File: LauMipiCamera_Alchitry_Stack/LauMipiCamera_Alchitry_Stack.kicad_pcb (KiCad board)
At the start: 2 copper layers, 55 x 45 mm, 19 parts, among them J1 DF40C-50DP (Site A / +3V3 onl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, J2 DF40C-80DP (Bank A / Site B /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, J3 DF40C-80DP (Bank B / Site C), SW1 SW_DIP_x4

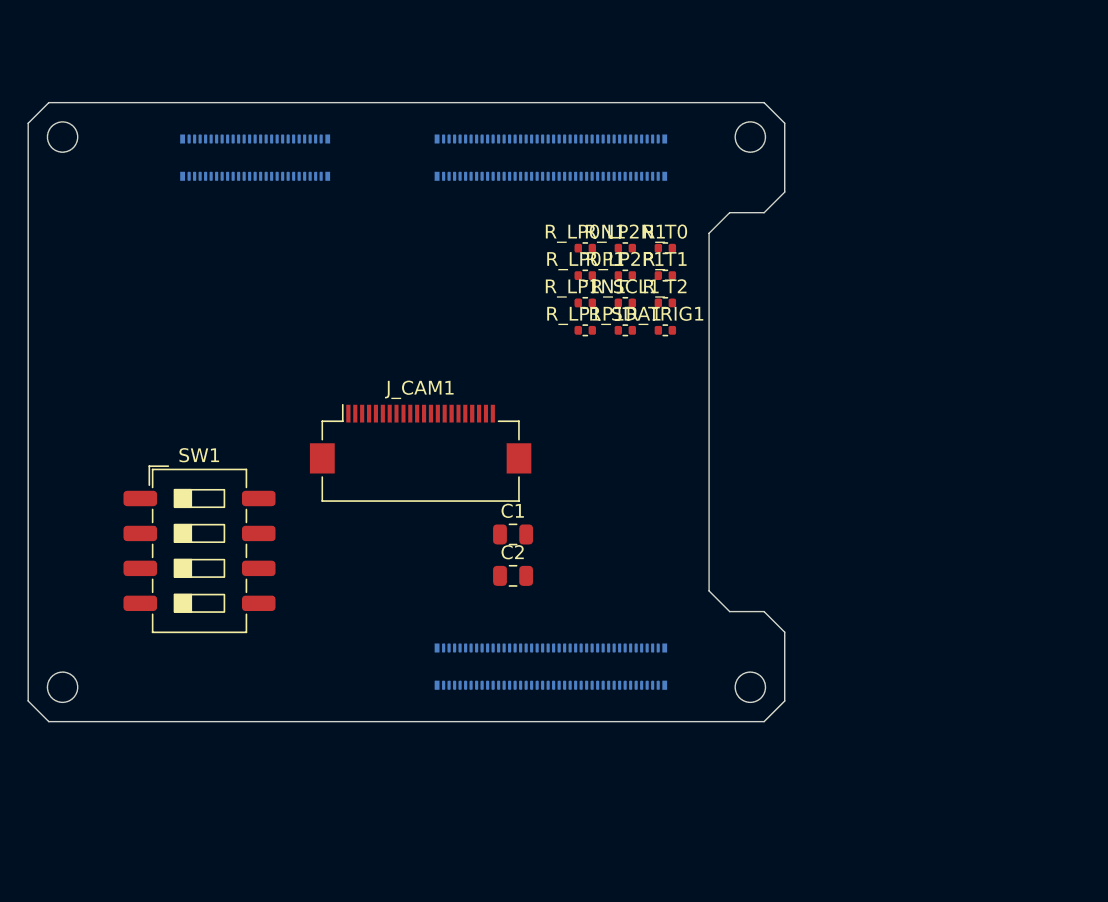
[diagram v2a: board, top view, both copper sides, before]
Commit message: hw(mipi): 4-layer stackup, 100R diff geometry, GND pours
Prerequisite for routing the D-PHY pairs. The board was 2-layer with no stackup
and no ground pour, so the HS pairs had no reference plane and 100 ohm
differential was unachievable (1.6 mm core would need ~1 mm traces, which cannot
escape a 0.4 mm-pitch DF40 fanout).

Stackup (generic 1.6 mm 4-layer, 1.62 mm with masks):
  F.Cu    35 um   signal   <- HS pairs, microstrip
    prepreg 0.0994 mm, er 4.45
  In1.Cu  15.2 um GND      <- reference plane
    core 1.3008 mm, er 4.6
  In2.Cu  15.2 um GND
    prepreg 0.0994 mm, er 4.45
  B.Cu    35 um   signal   <- DF40 plugs J1/J2/J3

100 ohm differential over that prepreg: trace 0.10 mm, gap 0.13 mm. Hammerstad
microstrip + Wadell coupling gives Zdiff = 101.9 ohm bare; solder mask pulls it
down ~2 ohm. Replaces the 0.13/0.13 placeholders in both .kicad_dru and the
MipiHS netclass. MUST still be confirmed against the fab's own stackup.

Added GND pours on all four layers (In1 highest priority -- it is the HS
reference). Zones are defined but not filled; fill in the GUI.

Also re-applied the MipiHS netclass clearance 0.2 -> 0.15 mm. KiCad had reverted
it when the project was saved from the GUI, which would have re-broken DRC
against the DF40's fixed 0.17 mm pad gap.

Documented in .kicad_dru that exactly ONE via per HS net is expected: J_CAM1 is
on F.Cu and J3 on B.Cu, so each pair drops through once near J3, swapping its
reference from In1 to In2 -- needs a GND stitching via beside each transition.

DRC: 0 copper violations, schematic_parity 0. 46 remaining are silkscreen.

Co-Authored-By: Claude Opus 4.8 (1M context) <noreply@anthropic.com>
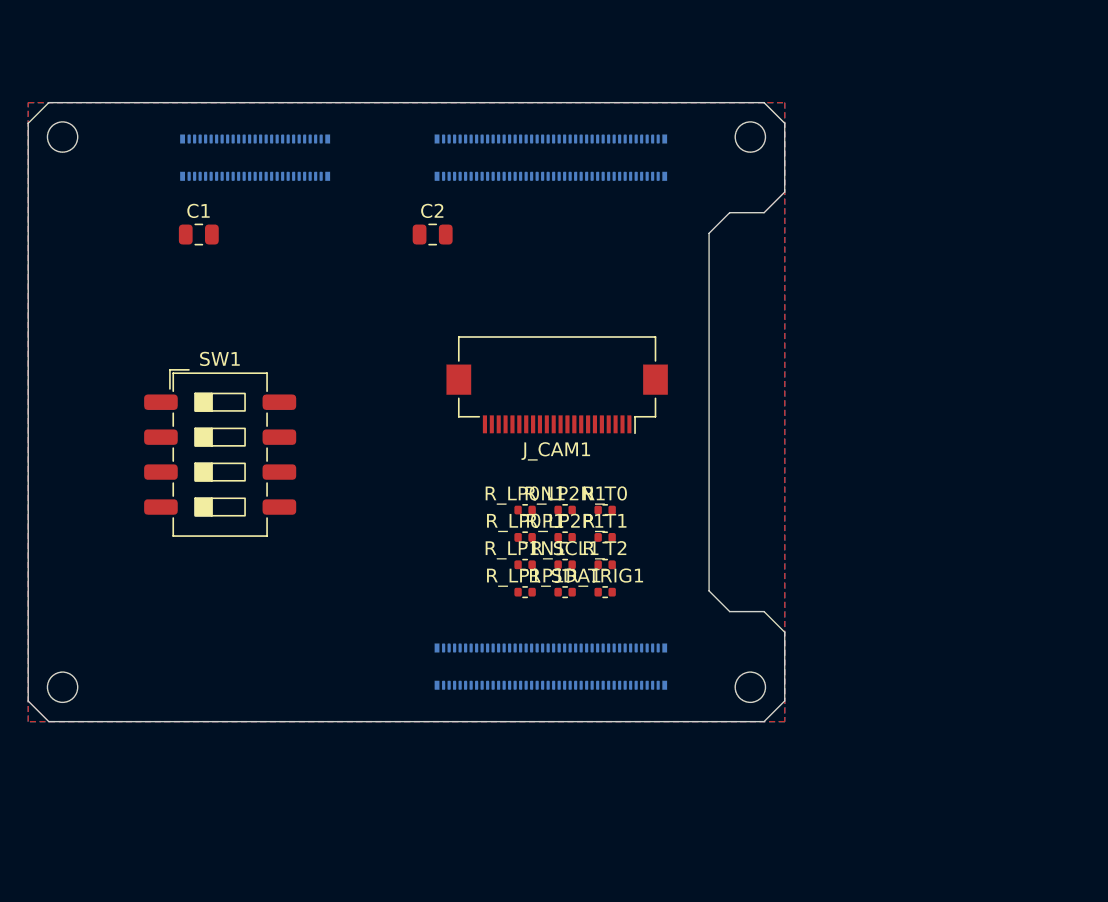
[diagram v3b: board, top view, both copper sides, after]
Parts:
- moved C1 31.6 mm to (131.9, 70.0)
- moved C2 25.5 mm to (148.9, 70.0)
- moved R_LP1N1 19.5 mm to (155.7, 94.0)
- moved R_SCL1 19.5 mm to (158.6, 94.0)
- moved R_T2 19.5 mm to (161.5, 94.0)
- moved R_LP0N1 19.5 mm to (155.7, 90.0)
- moved R_LP0P1 19.5 mm to (155.7, 92.0)
- moved R_LP1P1 19.5 mm to (155.7, 96.0)
- moved R_LP2N1 19.5 mm to (158.6, 90.0)
- moved R_LP2P1 19.5 mm to (158.6, 92.0)
- moved R_SDA1 19.5 mm to (158.6, 96.0)
- moved R_T0 19.5 mm to (161.5, 90.0)
- moved R_T1 19.5 mm to (161.5, 92.0)
- moved R_TRIG1 19.5 mm to (161.5, 96.0)
- moved J_CAM1 10.3 mm to (158.0, 82.0), turned to 180 degrees
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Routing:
- added copper zone on B.Cu, net GND
- added copper zone on F.Cu, net GND
- added copper zone on In1.Cu, net GND
- added copper zone on In2.Cu, net GND
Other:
- copper layers 2 -> 4

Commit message: hw(mipi): rotate J_CAM1 180 deg so the HS pairs stop crossing
All three D-PHY pairs crossed between the camera and J3:

  lane  at J_CAM1            at J3                verdict
  CK    P=159.25 N=159.75    P=158.94 N=158.54    P-left  vs P-right
  D0    P=162.25 N=162.75    P=157.75 N=157.34    P-left  vs P-right
  D1    P=160.75 N=161.25    P=158.94 N=158.54    P-left  vs P-right

Systematic, not a per-lane slip: J_CAM1 was at rot=180 so its pin numbers ran
right-to-left, while J3's run left-to-right. The FPGA side cannot absorb this --
on the DF40 the higher B-number is always the P ball (CK = B47/B45 -> V13/V14,
V13 = P; the spare MRCC pair B41/B39 has the same parity), so P is always to the
right. Swapping P/N in the schematic would land the camera's P on the FPGA's N.

Routing as-placed would need a crossover via on one leg of each pair: three
discontinuities mid-line on a 200 mV 691 Mb/s link, and it breaks the symmetry
that makes the 0.08 mm intra-pair skew constraint free.

Rotating J_CAM1 to rot=0 mirrors its pads about x=158. P now sits right of N on
all three lanes, matching J3, so each pair can be routed symmetric about its own
centreline and intra-pair skew is zero by construction. Cost: ~3.7 mm more run
per lane (camera pads y 83.80 -> 80.10) and the FFC cable exits the other side.

Also cleared the 180 deg self-rotation left on the 24 child pads, which had made
the footprint differ from its library copy (geometrically identical for rect
pads, but it raised lib_footprint_mismatch).

DRC: 0 copper violations, schematic_parity 0, 46 silkscreen.

Co-Authored-By: Claude Opus 4.8 (1M context) <noreply@anthropic.com>
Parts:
- turned J_CAM1 to 0 degrees
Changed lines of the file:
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@@
 	(footprint "Connector_FFC-FPC:Hirose_FH12-22S-0.5SH_1x22-1MP_P0.50mm_Horizontal"
 		(layer "F.Cu")
-		(at 158 81.95 180)
+		(at 158 81.95)
 		(descr "Hirose FH12, FFC/FPC connector, FH12-22S-0.5SH, 22 Pins per row (https://www.hirose.com/product/en/products/FH12/FH12-24S-0.5SH(55)/)")
 		(tags "connector Hirose FH12 horizontal")
@@
 		)
 		(pad "1" smd rect
-			(at -5.25 -1.85 180)
+			(at -5.25 -1.85)
 			(size 0.3 1.3)
 			(layers "F.Cu" "F.Mask" "F.Paste")
@@
 		)
 		(pad "2" smd rect
-			(at -4.75 -1.85 180)
+			(at -4.75 -1.85)
 			(size 0.3 1.3)
 			(layers "F.Cu" "F.Mask" "F.Paste")
@@
 		)
 		(pad "3" smd rect
-			(at -4.25 -1.85 180)
+			(at -4.25 -1.85)
 			(size 0.3 1.3)
 			(layers "F.Cu" "F.Mask" "F.Paste")
@@
 		)
 		(pad "4" smd rect
-			(at -3.75 -1.85 180)
+			(at -3.75 -1.85)
 			(size 0.3 1.3)
 			(layers "F.Cu" "F.Mask" "F.Paste")
@@
 		)
 		(pad "5" smd rect
-			(at -3.25 -1.85 180)
+			(at -3.25 -1.85)
 			(size 0.3 1.3)
 			(layers "F.Cu" "F.Mask" "F.Paste")
@@
 		)
 		(pad "6" smd rect
-			(at -2.75 -1.85 180)
+			(at -2.75 -1.85)
 			(size 0.3 1.3)
 			(layers "F.Cu" "F.Mask" "F.Paste")
@@
 		)
 		(pad "7" smd rect
-			(at -2.25 -1.85 180)
+			(at -2.25 -1.85)
 			(size 0.3 1.3)
 			(layers "F.Cu" "F.Mask" "F.Paste")
@@
 		)
 		(pad "8" smd rect
-			(at -1.75 -1.85 180)
+			(at -1.75 -1.85)
 			(size 0.3 1.3)
 			(layers "F.Cu" "F.Mask" "F.Paste")
@@
 		)
 		(pad "9" smd rect
-			(at -1.25 -1.85 180)
+			(at -1.25 -1.85)
 			(size 0.3 1.3)
 			(layers "F.Cu" "F.Mask" "F.Paste")
@@
 		)
 		(pad "10" smd rect
-			(at -0.75 -1.85 180)
+			(at -0.75 -1.85)
 			(size 0.3 1.3)
 			(layers "F.Cu" "F.Mask" "F.Paste")
@@
 		)
 		(pad "11" smd rect
-			(at -0.25 -1.85 180)
+			(at -0.25 -1.85)
 			(size 0.3 1.3)
 			(layers "F.Cu" "F.Mask" "F.Paste")
@@
 		)
 		(pad "12" smd rect
-			(at 0.25 -1.85 180)
+			(at 0.25 -1.85)
 			(size 0.3 1.3)
 			(layers "F.Cu" "F.Mask" "F.Paste")
@@
 		)
 		(pad "13" smd rect
-			(at 0.75 -1.85 180)
+			(at 0.75 -1.85)
 			(size 0.3 1.3)
 			(layers "F.Cu" "F.Mask" "F.Paste")
@@
 		)
 		(pad "14" smd rect
-			(at 1.25 -1.85 180)
+			(at 1.25 -1.85)
 			(size 0.3 1.3)
 			(layers "F.Cu" "F.Mask" "F.Paste")
@@
 		)
 		(pad "15" smd rect
-			(at 1.75 -1.85 180)
+			(at 1.75 -1.85)
 			(size 0.3 1.3)
 			(layers "F.Cu" "F.Mask" "F.Paste")
@@
 		)
 		(pad "16" smd rect
-			(at 2.25 -1.85 180)
+			(at 2.25 -1.85)
 			(size 0.3 1.3)
 			(layers "F.Cu" "F.Mask" "F.Paste")
@@
 		)
 		(pad "17" smd rect
-			(at 2.75 -1.85 180)
+			(at 2.75 -1.85)
 			(size 0.3 1.3)
 			(layers "F.Cu" "F.Mask" "F.Paste")
@@
 		)
 		(pad "18" smd rect
-			(at 3.25 -1.85 180)
+			(at 3.25 -1.85)
 			(size 0.3 1.3)
 			(layers "F.Cu" "F.Mask" "F.Paste")
@@
 		)
 		(pad "19" smd rect
-			(at 3.75 -1.85 180)
+			(at 3.75 -1.85)
 			(size 0.3 1.3)
 			(layers "F.Cu" "F.Mask" "F.Paste")
@@
 		)
 		(pad "20" smd rect
-			(at 4.25 -1.85 180)
+			(at 4.25 -1.85)
 			(size 0.3 1.3)
 			(layers "F.Cu" "F.Mask" "F.Paste")
@@
 		)
 		(pad "21" smd rect
-			(at 4.75 -1.85 180)
+			(at 4.75 -1.85)
 			(size 0.3 1.3)
 			(layers "F.Cu" "F.Mask" "F.Paste")
@@
 		)
 		(pad "22" smd rect
-			(at 5.25 -1.85 180)
+			(at 5.25 -1.85)
 			(size 0.3 1.3)
 			(layers "F.Cu" "F.Mask" "F.Paste")
@@
 		)
 		(pad "MP" smd rect
-			(at -7.15 1.4 180)
+			(at -7.15 1.4)
 			(size 1.8 2.2)
 			(layers "F.Cu" "F.Mask" "F.Paste")
 		)
 		(pad "MP" smd rect
-			(at 7.15 1.4 180)
+			(at 7.15 1.4)
 			(size 1.8 2.2)
 			(layers "F.Cu" "F.Mask" "F.Paste")

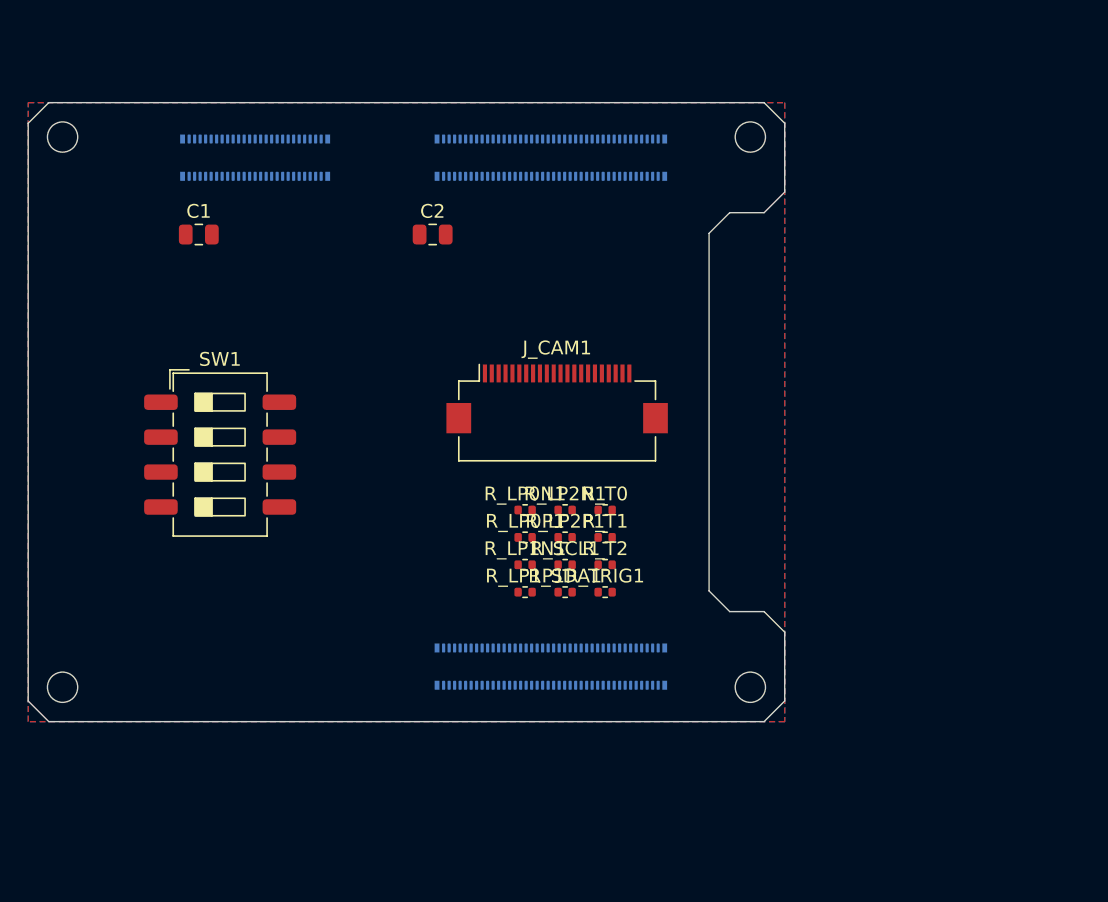
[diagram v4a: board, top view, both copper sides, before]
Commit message: hw(mipi): route the 4 DIP-switch nets and the +3V3 feed to C1/C2
31 segments, 5 vias. All four switch nets are fully connected end to end
(kicad-cli ratsnest: SW_HVSV / SW_BLUE / SW_GREEN / SW_RED all closed).

Topology. SW1's own GND pads (column at x=135.3) block a straight run east, and
J3's targets straddle both rows of a 0.4 mm-pitch connector, so:

  * each net takes a short F.Cu stub off SW1's west pad column
  * SW_HVSV and SW_GREEN drop to B.Cu beside the switch, run east under the
    board, and enter J3 through the INTER-ROW CORRIDOR (y 100.387..102.437 --
    empty between the even and odd pad rows), then turn south into pads 27/29.
    This is the escape the fabricated trigger board uses for its odd-row pins.
  * SW_BLUE and SW_RED stay on F.Cu, thread the gaps between SW1's GND pads
    (y 92.75..94.17 and 97.83..99.25), and drop to B.Cu north of J3 to enter
    pads 28/30 from above -- even-row pads face the board interior.

Lane order is nested so nothing crosses. First attempt put SW_GREEN's via west
of SW_HVSV's, which made GREEN's eastward lane cut straight through HVSV's
vertical (DRC: tracks_crossing). Moving GREEN's via east of HVSV's and hopping
SW_BLUE north through the pad gap fixed it.

+3V3: J1's five power pads (1/3/5/9/11) bus together on B.Cu, one via up, then
F.Cu out of J1's shadow to C1.1 and C2.1. Both caps' GND pads tie to the F.Cu
pour -- no track needed. The net's remaining three ratsnest legs (J_CAM1.22,
R_SCL1.1, R_SDA1.1) are deliberately left for later.

DRC: 0 copper violations, schematic_parity 0, 46 silkscreen. Ratsnest 112 -> 102.
GND still shows ratsnest because the zones are defined but not filled -- there is
no CLI fill; press B in the GUI.

Co-Authored-By: Claude Opus 4.8 (1M context) <noreply@anthropic.com>
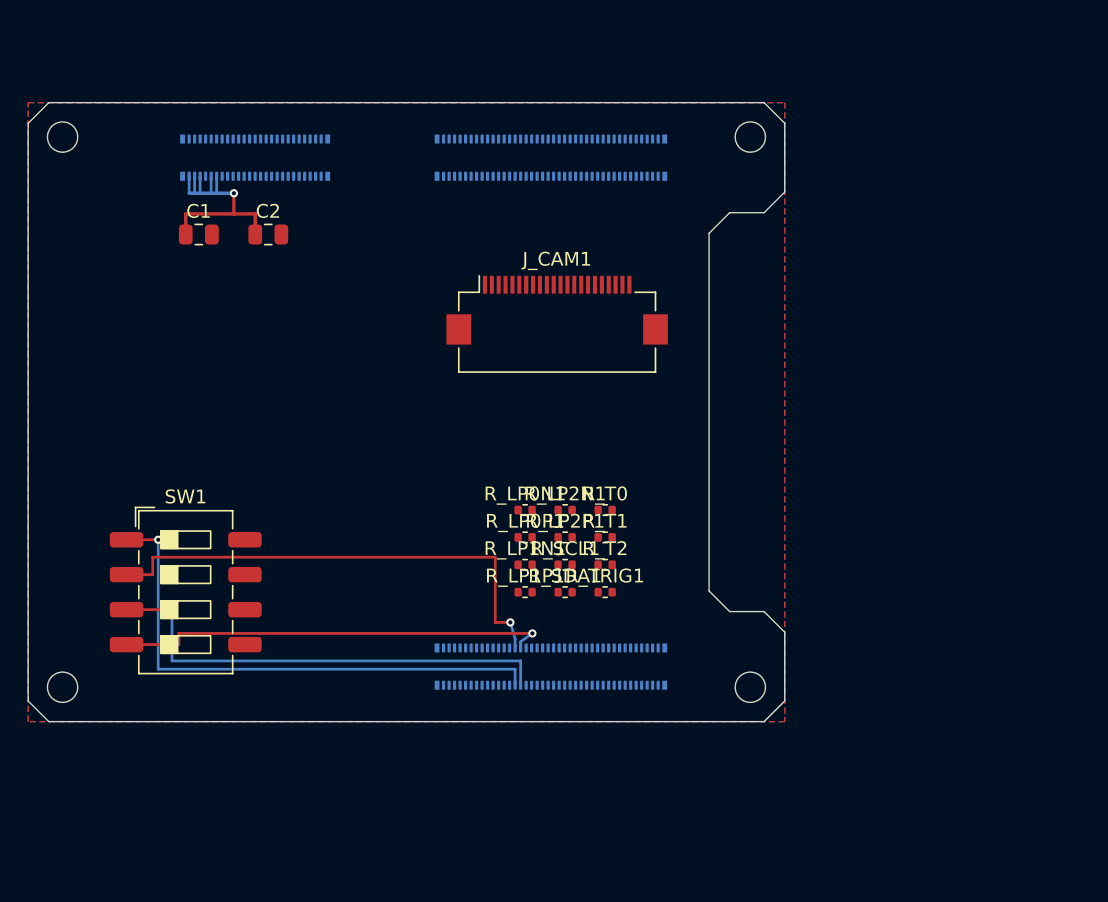
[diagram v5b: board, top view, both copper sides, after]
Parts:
- moved C2 11.9 mm to (137.0, 70.0)
- moved SW1 10.3 mm to (131.0, 96.0)
- moved J_CAM1 6.45 mm to (158.0, 75.5)
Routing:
- net SW_HVSV: track 0.00 -> 38.8 mm, vias 0 -> 1
- net SW_BLUE: track 0.00 -> 35.8 mm, vias 0 -> 1
- net SW_GREEN: track 0.00 -> 34.1 mm, vias 0 -> 1
- net SW_RED: track 0.00 -> 31.8 mm, vias 0 -> 1
- net +3V3: track 0.00 -> 19.0 mm, vias 0 -> 1
